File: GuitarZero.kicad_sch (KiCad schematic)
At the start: 9 parts, among them J1 AudioJack3_Ground_SwitchTR, J2 USB_B_Micro, SW1 SW_Push, SW2 SW_Push, SW3 SW_Push, SW4 SW_Push, SW5 SW_Push, SW6 SW_Push

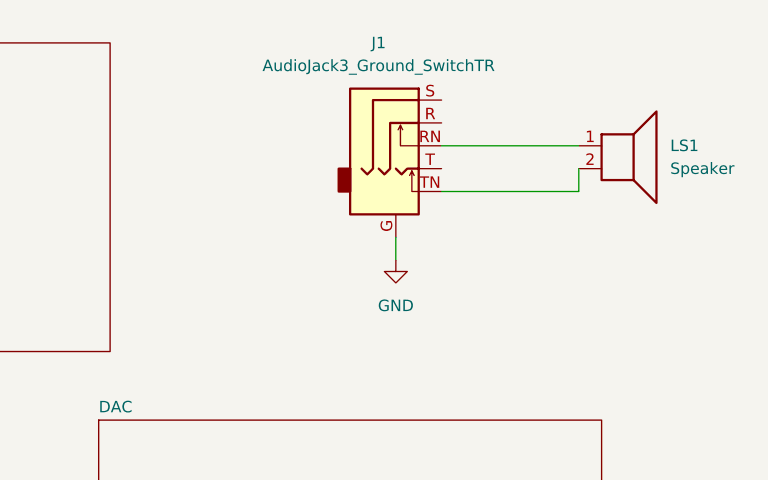
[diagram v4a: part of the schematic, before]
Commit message: Swapped to 3-pin jack with switch
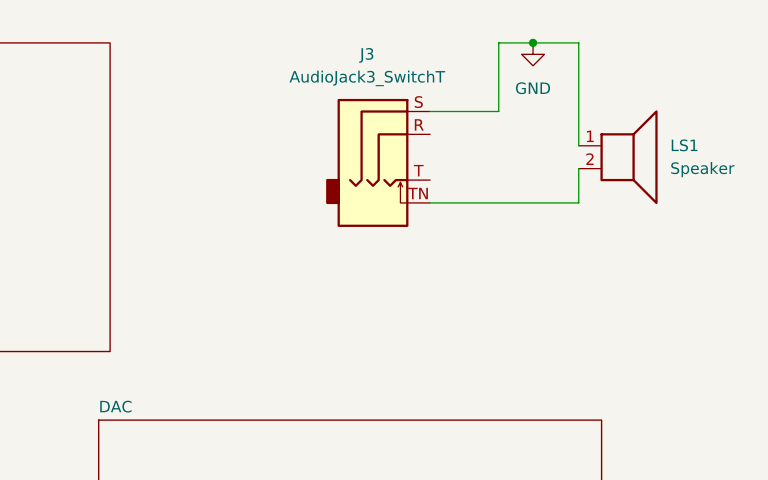
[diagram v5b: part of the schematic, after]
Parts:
- removed J1: AudioJack3_Ground_SwitchTR, symbol Connector_Audio:AudioJack3_Ground_SwitchTR
- added J3: AudioJack3_SwitchT, symbol Connector_Audio:AudioJack3_SwitchT
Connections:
- net GND: now also LS1.1, J3.S
- net at LS1.2: now also J3.TN
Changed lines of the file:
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@@
 (kicad_sch (version 20230121) (generator eeschema)
   (paper "A4")
+  (junction (at 232.41 25.4) (diameter 0) (color 0 0 0 0)
+  )
   (junction (at 53.34 55.88) (diameter 0) (color 0 0 0 0)
   )
@@
     (stroke (width 0) (type default))
   )
-  (wire (pts (xy 237.49 41.91) (xy 237.49 39.37))
-    (stroke (width 0) (type default))
-  )
   (wire (pts (xy 24.13 162.56) (xy 27.94 162.56))
     (stroke (width 0) (type default))
   )
-  (wire (pts (xy 222.25 41.91) (xy 237.49 41.91))
-    (stroke (width 0) (type default))
-  )
   (wire (pts (xy 24.13 120.65) (xy 24.13 132.08))
     (stroke (width 0) (type default))
@@
     (stroke (width 0) (type default))
   )
+  (wire (pts (xy 237.49 36.83) (xy 237.49 25.4))
+    (stroke (width 0) (type default))
+  )
   (wire (pts (xy 30.48 48.26) (xy 27.94 48.26))
     (stroke (width 0) (type default))
@@
     (stroke (width 0) (type default))
   )
+  (wire (pts (xy 220.98 33.02) (xy 228.6 33.02))
+    (stroke (width 0) (type default))
+  )
   (wire (pts (xy 24.13 132.08) (xy 24.13 142.24))
     (stroke (width 0) (type default))
@@
     (stroke (width 0) (type default))
   )
-  (wire (pts (xy 217.17 46.99) (xy 217.17 49.53))
+  (wire (pts (xy 237.49 25.4) (xy 232.41 25.4))
     (stroke (width 0) (type default))
   )
@@
     (stroke (width 0) (type default))
   )
+  (wire (pts (xy 237.49 39.37) (xy 237.49 43.18))
+    (stroke (width 0) (type default))
+  )
   (wire (pts (xy 24.13 142.24) (xy 24.13 152.4))
     (stroke (width 0) (type default))
   )
-  (wire (pts (xy 222.25 36.83) (xy 237.49 36.83))
+  (wire (pts (xy 228.6 33.02) (xy 228.6 25.4))
     (stroke (width 0) (type default))
   )
@@
     (stroke (width 0) (type default))
   )
+  (wire (pts (xy 220.98 43.18) (xy 237.49 43.18))
+    (stroke (width 0) (type default))
+  )
   (wire (pts (xy 24.13 172.72) (xy 27.94 172.72))
+    (stroke (width 0) (type default))
+  )
+  (wire (pts (xy 228.6 25.4) (xy 232.41 25.4))
     (stroke (width 0) (type default))
   )
   (text "Power Out" (at 44.45 43.18 0)
     (effects (font (size 1.27 1.27)) (justify left bottom))
+  )
+  (symbol (lib_id "Connector_Audio:AudioJack3_SwitchT") (at 215.9 35.56 0) (unit 1)
+    (in_bom yes) (on_board yes) (dnp no) (fields_autoplaced)
+    (property "Reference" "J3" (at 213.995 26.67 0)
+      (effects (font (size 1.27 1.27)))
+    )
+    (property "Value" "AudioJack3_SwitchT" (at 213.995 29.21 0)
+      (effects (font (size 1.27 1.27)))
+    )
+    (property "Footprint" "" (at 215.9 35.56 0)
+      (effects (font (size 1.27 1.27)) hide)
+    )
+    (property "Datasheet" "~" (at 215.9 35.56 0)
+      (effects (font (size 1.27 1.27)) hide)
+    )
+    (pin "R")
+    (pin "S")
+    (pin "T")
+    (pin "TN")
+    (instances
+      (project "GuitarZero"
+        (path "/fba50eda-8593-4456-af98-ff56fd418a76"
+          (reference "J3") (unit 1)
+        )
+      )
+    )
   )
   (symbol (lib_id "power:+5V") (at 46.99 27.94 0) (unit 1)
@@
     )
   )
-  (symbol (lib_id "power:GND") (at 217.17 49.53 0) (unit 1)
-    (in_bom yes) (on_board yes) (dnp no) (fields_autoplaced)
-    (property "Reference" "#PWR033" (at 217.17 55.88 0)
-      (effects (font (size 1.27 1.27)) hide)
-    )
-    (property "Value" "GND" (at 217.17 54.61 0)
-      (effects (font (size 1.27 1.27)))
-    )
-    (property "Footprint" "" (at 217.17 49.53 0)
-      (effects (font (size 1.27 1.27)) hide)
-    )
-    (property "Datasheet" "" (at 217.17 49.53 0)
+  (symbol (lib_id "power:GND") (at 232.41 25.4 0) (unit 1)
+    (in_bom yes) (on_board yes) (dnp no) (fields_autoplaced)
+    (property "Reference" "#PWR033" (at 232.41 31.75 0)
+      (effects (font (size 1.27 1.27)) hide)
+    )
+    (property "Value" "GND" (at 232.41 30.48 0)
+      (effects (font (size 1.27 1.27)))
+    )
+    (property "Footprint" "" (at 232.41 25.4 0)
+      (effects (font (size 1.27 1.27)) hide)
+    )
+    (property "Datasheet" "" (at 232.41 25.4 0)
       (effects (font (size 1.27 1.27)) hide)
     )
@@
         )
       )
-    )
-  )
-  (symbol (lib_id "Connector_Audio:AudioJack3_Ground_SwitchTR") (at 217.17 34.29 0) (unit 1)
-    (in_bom yes) (on_board yes) (dnp no) (fields_autoplaced)
-    (property "Reference" "J1" (at 215.265 25.4 0)
-      (effects (font (size 1.27 1.27)))
-    )
-    (property "Value" "AudioJack3_Ground_SwitchTR" (at 215.265 27.94 0)
-      (effects (font (size 1.27 1.27)))
-    )
-    (property "Footprint" "" (at 217.17 34.29 0)
-      (effects (font (size 1.27 1.27)) hide)
-    )
-    (property "Datasheet" "~" (at 217.17 34.29 0)
-      (effects (font (size 1.27 1.27)) hide)
-    )
-    (pin "G")
-    (pin "R")
-    (pin "RN")
-    (pin "S")
-    (pin "T")
-    (pin "TN")
-    (instances
-      (project "GuitarZero"
-        (path "/fba50eda-8593-4456-af98-ff56fd418a76"
-          (reference "J1") (unit 1)
-        )
-      )

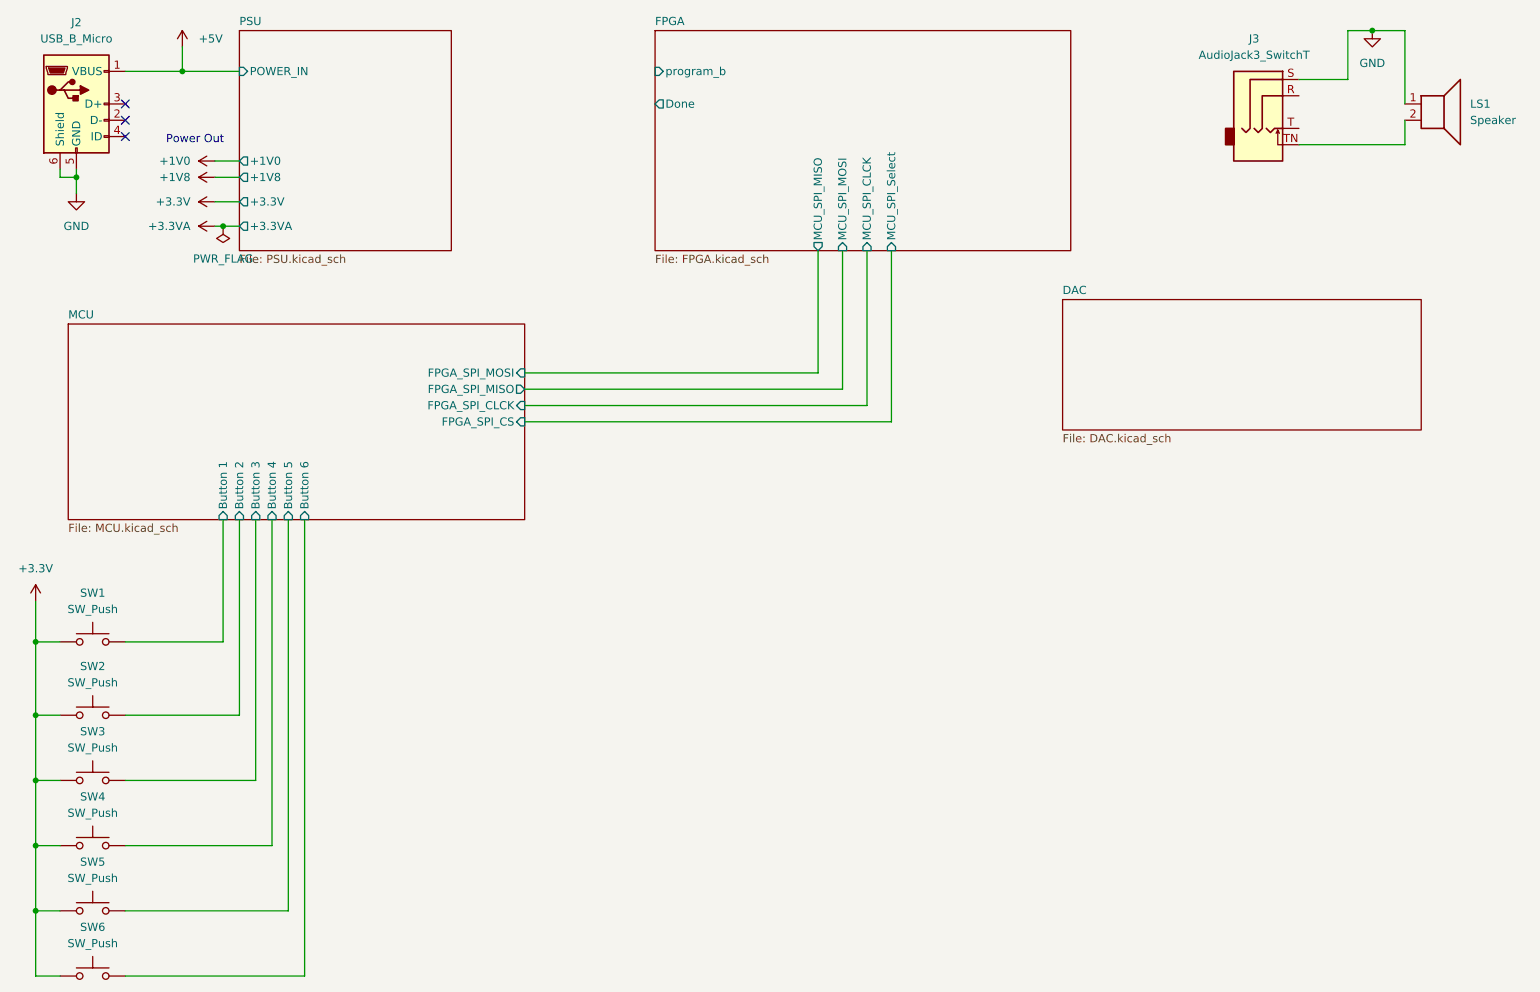
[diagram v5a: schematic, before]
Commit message: Connected FPGA and DAC
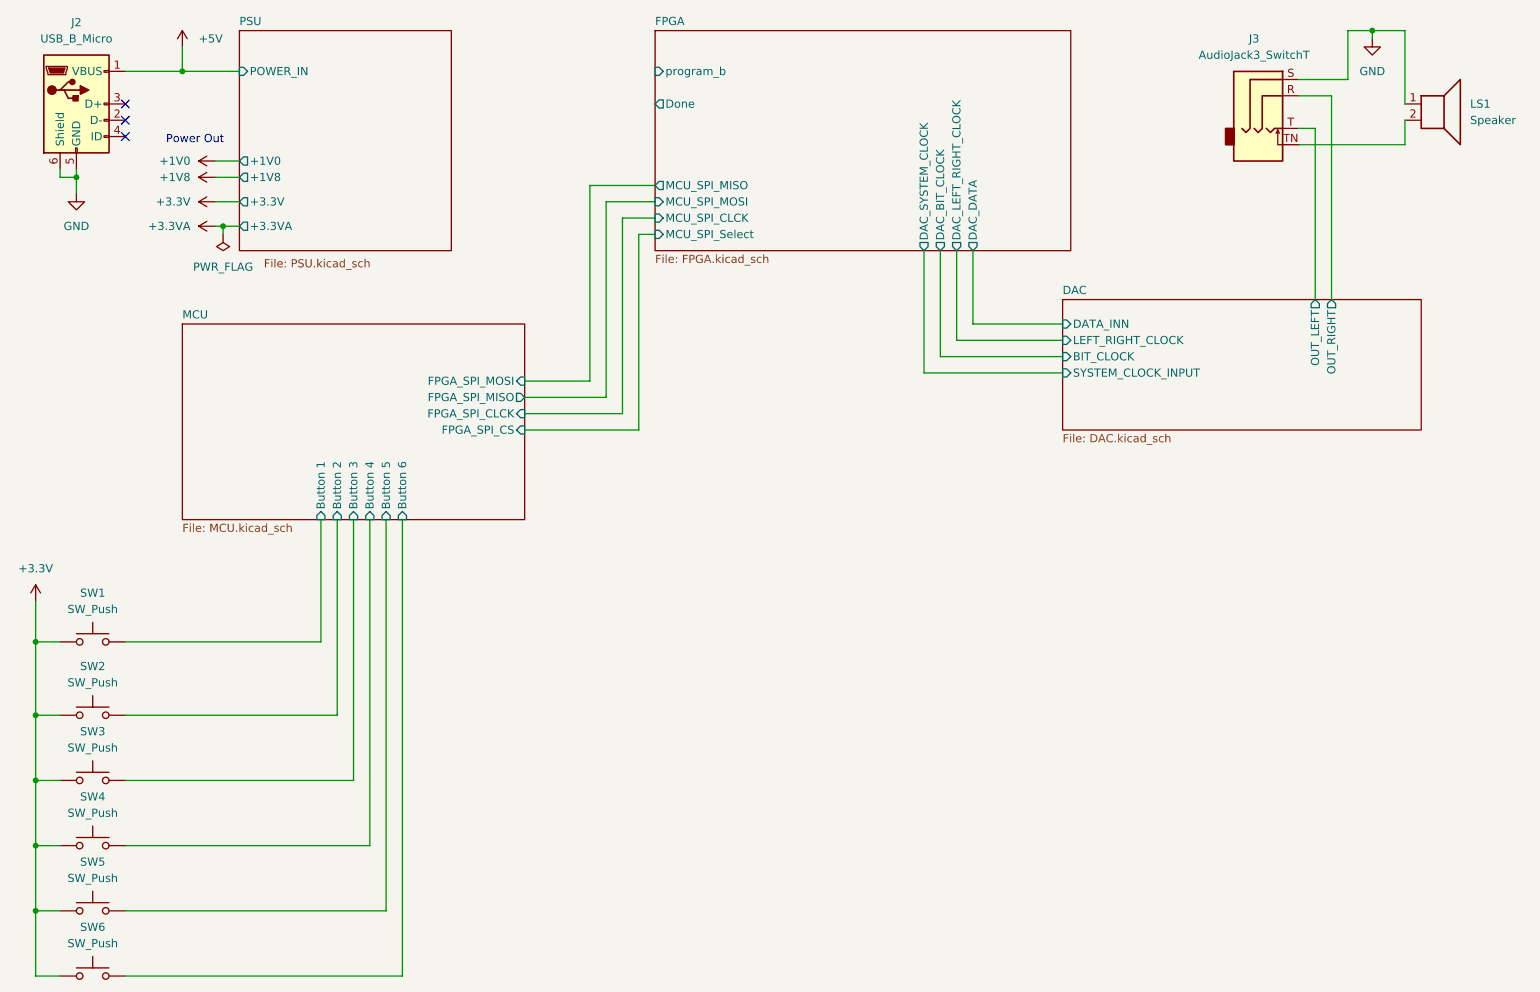
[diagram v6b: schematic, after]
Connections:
- net DAC/OUT_RIGHT: now reaches J3.R
- net DAC/OUT_LEFT: now reaches J3.T
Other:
- sheet DAC ports: added BIT_CLOCK, DATA_INN, LEFT_RIGHT_CLOCK, OUT_LEFT, OUT_RIGHT, SYSTEM_CLOCK_INPUT; removed none
- sheet FPGA ports: added DAC_BIT_CLOCK, DAC_DATA, DAC_LEFT_RIGHT_CLOCK, DAC_SYSTEM_CLOCK; removed none

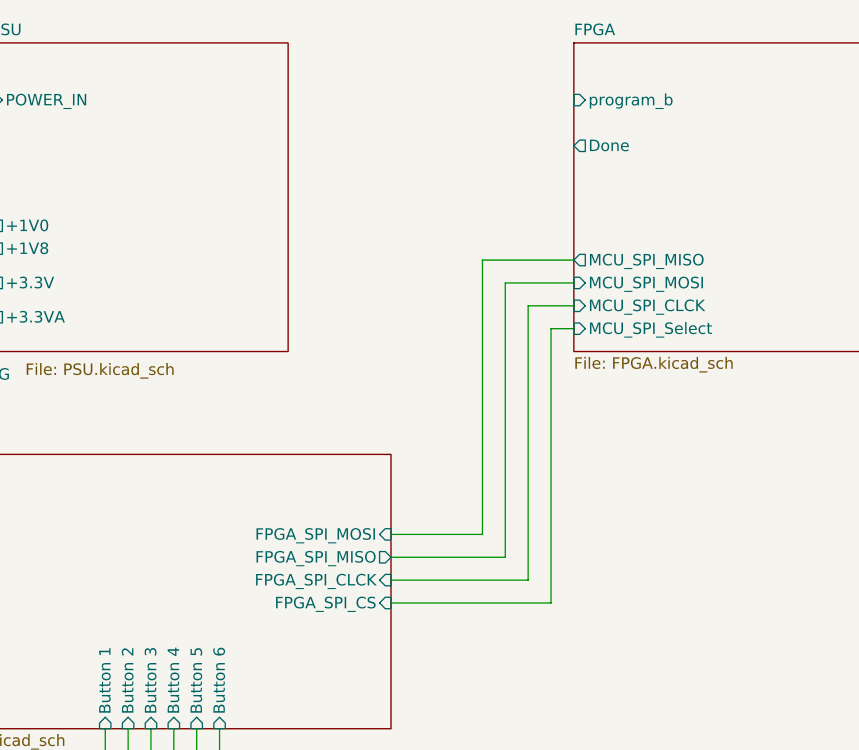
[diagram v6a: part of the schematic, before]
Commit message: Wired FPGA program to MCU
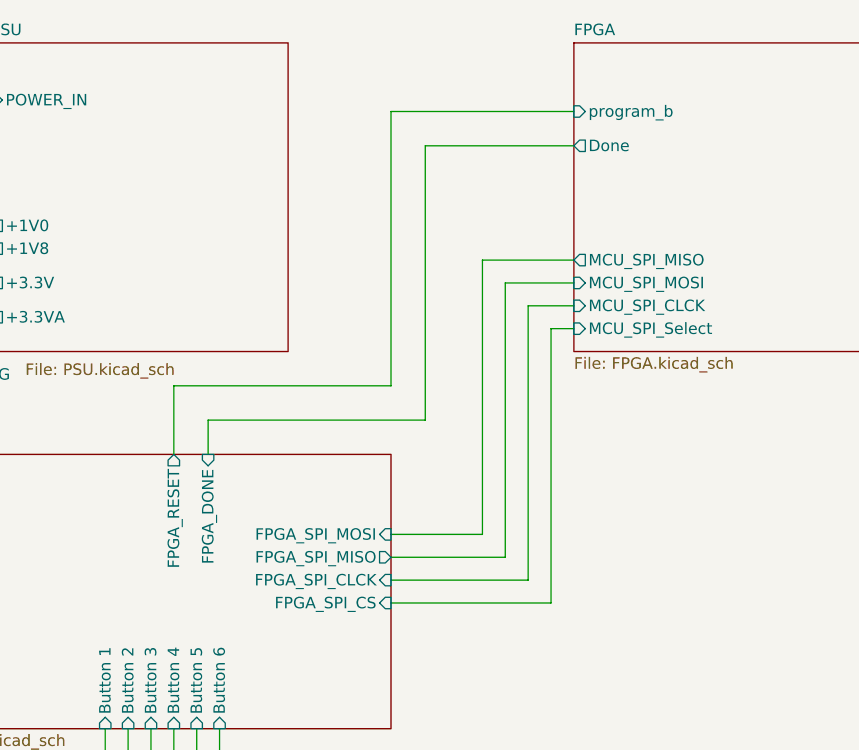
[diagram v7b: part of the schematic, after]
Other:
- sheet MCU ports: added FPGA_DONE, FPGA_RESET; removed none
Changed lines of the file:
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@@
+    (stroke (width 0) (type default))
+  )
+  (wire (pts (xy 100.33 33.02) (xy 120.65 33.02))
     (stroke (width 0) (type default))
   )
@@
     (stroke (width 0) (type default))
   )
+  (wire (pts (xy 100.33 63.5) (xy 100.33 33.02))
+    (stroke (width 0) (type default))
+  )
   (wire (pts (xy 162.56 59.69) (xy 162.56 78.74))
     (stroke (width 0) (type default))
@@
     (stroke (width 0) (type default))
   )
+  (wire (pts (xy 76.2 63.5) (xy 100.33 63.5))
+    (stroke (width 0) (type default))
+  )
   (wire (pts (xy 30.48 48.26) (xy 27.94 48.26))
     (stroke (width 0) (type default))
@@
     (stroke (width 0) (type default))
   )
+  (wire (pts (xy 104.14 36.83) (xy 120.65 36.83))
+    (stroke (width 0) (type default))
+  )
   (wire (pts (xy 24.13 114.3) (xy 24.13 120.65))
     (stroke (width 0) (type default))
@@
     (stroke (width 0) (type default))
   )
+  (wire (pts (xy 104.14 67.31) (xy 104.14 36.83))
+    (stroke (width 0) (type default))
+  )
   (wire (pts (xy 24.13 142.24) (xy 24.13 152.4))
     (stroke (width 0) (type default))
@@
     (stroke (width 0) (type default))
   )
+  (wire (pts (xy 80.01 67.31) (xy 104.14 67.31))
+    (stroke (width 0) (type default))
+  )
+  (wire (pts (xy 80.01 71.12) (xy 80.01 67.31))
+    (stroke (width 0) (type default))
+  )
   (wire (pts (xy 24.13 132.08) (xy 27.94 132.08))
     (stroke (width 0) (type default))
@@
   )
   (wire (pts (xy 24.13 152.4) (xy 27.94 152.4))
+    (stroke (width 0) (type default))
+  )
+  (wire (pts (xy 76.2 71.12) (xy 76.2 63.5))
     (stroke (width 0) (type default))
   )
@@
       (effects (font (size 1.27 1.27)) (justify left top))
     )
-    (pin "program_b" input (at 120.65 31.75 180)
+    (pin "program_b" input (at 120.65 33.02 180)
       (effects (font (size 1.27 1.27)) (justify left))
     )
@@
       (effects (font (size 1.27 1.27)) (justify left))
     )
-    (instances
+    (pin "FPGA_DONE" input (at 80.01 71.12 90)
+      (effects (font (size 1.27 1.27)) (justify right))
+    )
+    (pin "FPGA_RESET" output (at 76.2 71.12 90)
+      (effects (font (size 1.27 1.27)) (justify right))
+    )
+    (instances
